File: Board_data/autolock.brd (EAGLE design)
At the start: 65 x 56 mm, 10 parts, among them CN1 RASPBERRYPI-GPIO

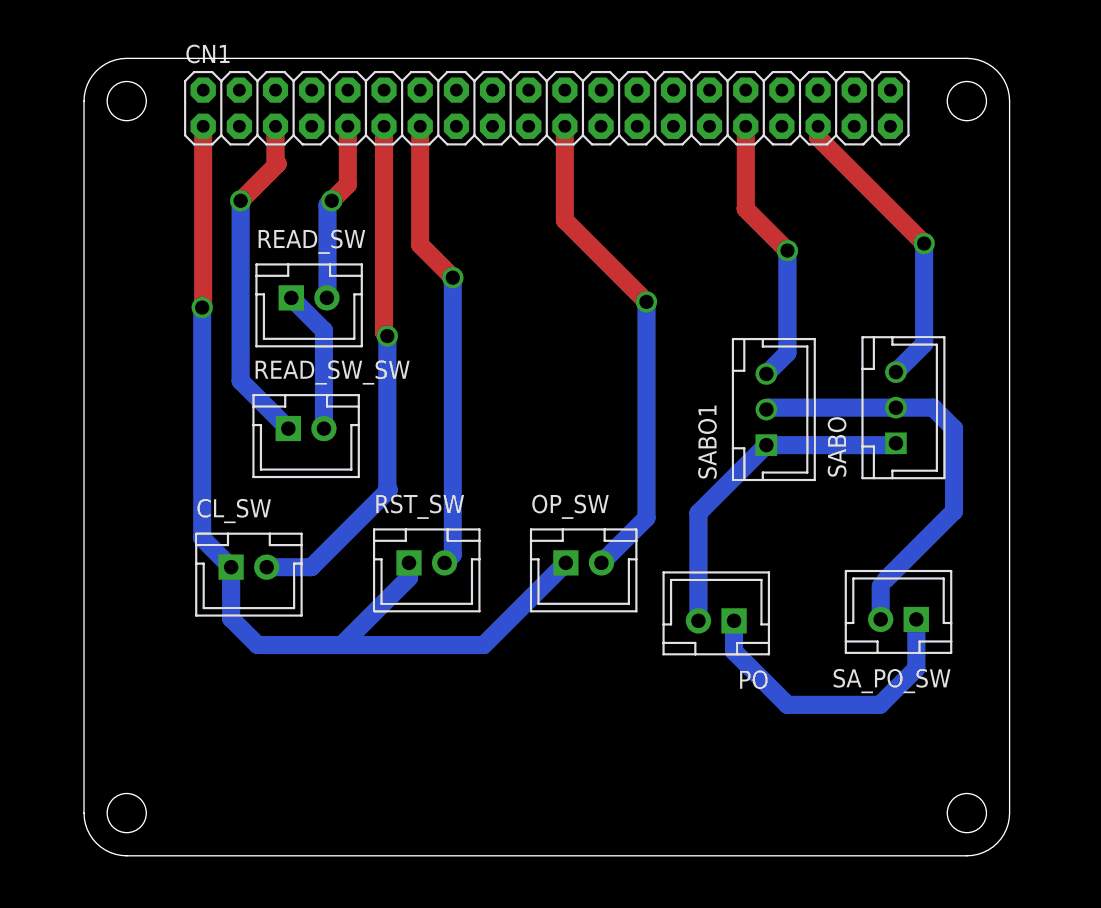
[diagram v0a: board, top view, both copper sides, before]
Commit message: 基板修正・リードスイッチ調整
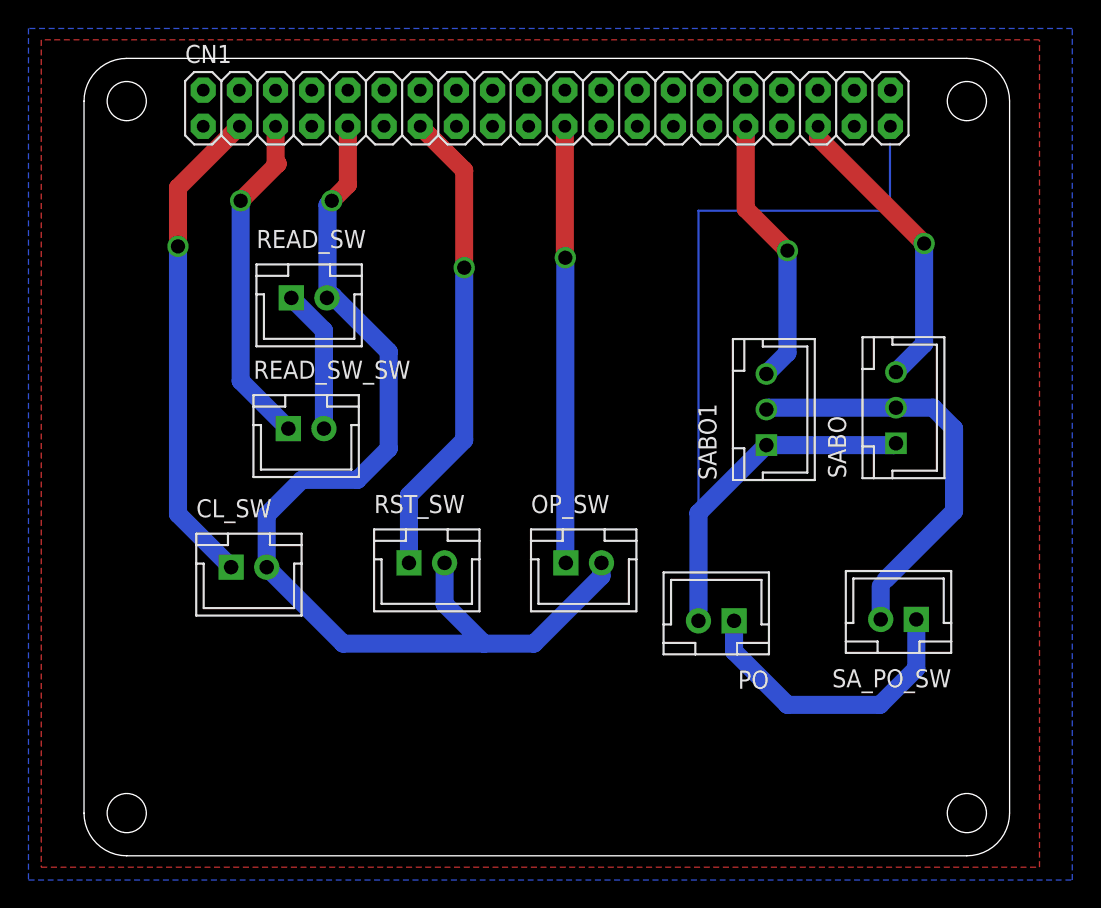
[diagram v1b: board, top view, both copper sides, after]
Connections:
- removed net N$12: PO.2, SABO.1, SABO1.1
- removed net N$4: CN1.9, READ_SW.2
- removed net N$8: CL_SW.2, CN1.11
- removed net N$9: CN1.13, RST_SW.2
- new net GND: CL_SW.2, CN1.39, CN1.9, OP_SW.2, PO.2, READ_SW.2, RST_SW.2, SABO.1, SABO1.1
- new net N$14: CN1.13, RST_SW.1
- net N$1: now also CN1.21; no longer CL_SW.1, CN1.1, RST_SW.1
- net N$2: now also CL_SW.1, CN1.3; no longer CN1.21, OP_SW.2
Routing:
- net GND: track 0.00 -> 145.3 mm, vias 0 -> 1
- net N$1: track 69.8 -> 30.7 mm
- net N$8: track 36.5 -> 0.00 mm, vias 1 -> 0
- net N$14: track 0.00 -> 33.5 mm, vias 0 -> 1
- net N$9: track 31.8 -> 0.00 mm, vias 1 -> 0
- net N$12: track 23.5 -> 0.00 mm
- net N$4: track 12.5 -> 0.00 mm, vias 1 -> 0
- added copper zone on layer 1, net GND
- added copper zone on layer 16, net GND
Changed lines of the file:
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@@
 <signal name="N$1">
 <contactref element="OP_SW" pad="1"/>
-<contactref element="CN1" pad="1"/>
-<contactref element="RST_SW" pad="1"/>
-<contactref element="CL_SW" pad="1"/>
-<wire x1="8.37" y1="51.23" x2="8.37" y2="38.57" width="1.27" layer="1"/>
-<wire x1="8.37" y1="38.57" x2="8.3" y2="38.5" width="1.27" layer="1"/>
-<via x="8.3" y="38.5" extent="1-16" drill="1" diameter="0.3"/>
-<wire x1="8.3" y1="38.5" x2="8.3" y2="22.3" width="1.27" layer="16"/>
-<wire x1="8.3" y1="22.3" x2="10.33" y2="20.27" width="1.27" layer="16"/>
-<wire x1="10.33" y1="20.27" x2="10.33" y2="16.67" width="1.27" layer="16"/>
-<wire x1="10.33" y1="16.67" x2="12.2" y2="14.8" width="1.27" layer="16"/>
-<wire x1="12.2" y1="14.8" x2="18.1" y2="14.8" width="1.27" layer="16"/>
-<wire x1="18.1" y1="14.8" x2="22.82" y2="19.52" width="1.27" layer="16"/>
-<wire x1="22.82" y1="19.52" x2="22.82" y2="20.57" width="1.27" layer="16"/>
-<wire x1="18.1" y1="14.8" x2="28.07" y2="14.8" width="1.27" layer="16"/>
-<wire x1="28.07" y1="14.8" x2="33.84" y2="20.57" width="1.27" layer="16"/>
-</signal>
-<signal name="N$2">
-<contactref element="OP_SW" pad="2"/>
 <contactref element="CN1" pad="21"/>
-<wire x1="33.77" y1="51.23" x2="33.77" y2="44.63" width="1.27" layer="1"/>
-<wire x1="33.77" y1="44.63" x2="39.5" y2="38.9" width="1.27" layer="1"/>
-<via x="39.5" y="38.9" extent="1-16" drill="1" diameter="0.3"/>
-<wire x1="39.5" y1="38.9" x2="39.5" y2="23.73" width="1.27" layer="16"/>
-<wire x1="39.5" y1="23.73" x2="36.34" y2="20.57" width="1.27" layer="16"/>
+<wire x1="33.77" y1="51.23" x2="33.77" y2="42.03" width="1.27" layer="1"/>
+<wire x1="33.77" y1="42.03" x2="33.8" y2="42" width="1.27" layer="1"/>
+<via x="33.8" y="42" extent="1-16" drill="1" diameter="0.3"/>
+<wire x1="33.8" y1="42" x2="33.8" y2="20.61" width="1.27" layer="16"/>
+<wire x1="33.8" y1="20.61" x2="33.84" y2="20.57" width="1.27" layer="16"/>
 </signal>
 <signal name="N$3">
@@
 <wire x1="11" y1="33.35" x2="14.35" y2="30" width="1.27" layer="16"/>
 </signal>
-<signal name="N$4">
-<contactref element="CN1" pad="9"/>
-<wire x1="18.53" y1="51.23" x2="18.53" y2="47.13" width="1.27" layer="1"/>
-<wire x1="18.53" y1="47.13" x2="17.4" y2="46" width="1.27" layer="1"/>
-<via x="17.4" y="46" extent="1-16" drill="1" diameter="0.3"/>
-<wire x1="17.4" y1="46" x2="17.1" y2="45.7" width="1.27" layer="16"/>
-<wire x1="17.1" y1="45.7" x2="17.1" y2="39.32" width="1.27" layer="16"/>
-<contactref element="READ_SW" pad="2"/>
-<wire x1="17.06" y1="39.18" x2="17.1" y2="39.32" width="0" layer="19" extent="16-16"/>
-</signal>
 <signal name="N$7">
 <contactref element="CN1" pad="35"/>
@@
 <wire x1="59" y1="43" x2="59" y2="35.95" width="1.27" layer="16"/>
 <wire x1="59" y1="35.95" x2="57.02" y2="33.97" width="1.27" layer="16"/>
-</signal>
-<signal name="N$9">
-<contactref element="RST_SW" pad="2"/>
-<contactref element="CN1" pad="13"/>
-<wire x1="23.61" y1="51.23" x2="23.61" y2="42.89" width="1.27" layer="1"/>
-<wire x1="23.61" y1="42.89" x2="25.9" y2="40.6" width="1.27" layer="1"/>
-<via x="25.9" y="40.6" extent="1-16" drill="1" diameter="0.3"/>
-<wire x1="25.9" y1="40.6" x2="25.9" y2="21.15" width="1.27" layer="16"/>
-<wire x1="25.9" y1="21.15" x2="25.32" y2="20.57" width="1.27" layer="16"/>
 </signal>
 <signal name="N$6">
@@
 <wire x1="55.95" y1="18.95" x2="56.3" y2="19.4" width="0" layer="19" extent="16-16"/>
 </signal>
-<signal name="N$8">
-<contactref element="CL_SW" pad="2"/>
-<contactref element="CN1" pad="11"/>
-<via x="21.3" y="36.5" extent="1-16" drill="1" diameter="0.3"/>
-<wire x1="12.83" y1="20.27" x2="15.97" y2="20.27" width="1.27" layer="16"/>
-<wire x1="21.4" y1="25.7" x2="15.97" y2="20.27" width="1.27" layer="16"/>
-<wire x1="21.07" y1="51.23" x2="21.07" y2="36.73" width="1.27" layer="1"/>
-<wire x1="21.07" y1="36.73" x2="21.3" y2="36.5" width="1.27" layer="1"/>
-<wire x1="21.3" y1="36.5" x2="21.3" y2="25.8" width="1.27" layer="16"/>
-<wire x1="21.3" y1="25.8" x2="21.4" y2="25.7" width="1.27" layer="16"/>
-</signal>
 <signal name="N$10">
 <contactref element="SABO1" pad="3"/>
@@
 <wire x1="49.4" y1="42.5" x2="49.4" y2="35.3195375" width="1.27" layer="16"/>
 <wire x1="49.4" y1="35.3195375" x2="47.92" y2="33.84" width="1.27" layer="16"/>
-</signal>
-<signal name="N$12">
-<contactref element="SABO" pad="1"/>
-<contactref element="SABO1" pad="1"/>
-<wire x1="57.02" y1="28.97" x2="56.89" y2="28.84" width="1.27" layer="16"/>
-<wire x1="56.89" y1="28.84" x2="47.92" y2="28.84" width="1.27" layer="16"/>
-<contactref element="PO" pad="2"/>
-<wire x1="47.92" y1="28.84" x2="43.15" y2="24.07" width="1.27" layer="16"/>
-<wire x1="43.15" y1="24.07" x2="43.15" y2="16.5" width="1.27" layer="16"/>
 </signal>
 <signal name="N$5">
@@
 <wire x1="16.85" y1="36.89" x2="16.85" y2="30" width="1.27" layer="16"/>
 </signal>
+<signal name="N$14">
+<contactref element="RST_SW" pad="1"/>
+<contactref element="CN1" pad="13"/>
+<wire x1="23.61" y1="51.23" x2="26.7" y2="48.14" width="1.27" layer="1"/>
+<wire x1="26.7" y1="48.14" x2="26.7" y2="41.3" width="1.27" layer="1"/>
+<via x="26.7" y="41.3" extent="1-16" drill="1" diameter="0.3"/>
+<wire x1="26.7" y1="41.3" x2="26.7" y2="29.2" width="1.27" layer="16"/>
+<wire x1="22.82" y1="25.32" x2="22.82" y2="20.57" width="1.27" layer="16"/>
+<wire x1="26.7" y1="29.2" x2="22.82" y2="25.32" width="1.27" layer="16"/>
+</signal>
+<signal name="N$2">
+<contactref element="CL_SW" pad="1"/>
+<contactref element="CN1" pad="3"/>
+<wire x1="10.91" y1="51.23" x2="6.6" y2="46.92" width="1.27" layer="1"/>
+<wire x1="6.6" y1="46.92" x2="6.6" y2="42.8" width="1.27" layer="1"/>
+<via x="6.6" y="42.8" extent="1-16" drill="1" diameter="0.3"/>
+<wire x1="6.6" y1="42.8" x2="6.6" y2="24" width="1.27" layer="16"/>
+<wire x1="6.6" y1="24" x2="10.33" y2="20.27" width="1.27" layer="16"/>
+</signal>
+<signal name="GND">
+<polygon width="0.1524" layer="1" isolate="0.4">
+<vertex x="-3" y="57.3"/>
+<vertex x="-3" y="-0.8"/>
+<vertex x="67.1" y="-0.8"/>
+<vertex x="67.1" y="57.3"/>
+</polygon>
+<polygon width="0.1524" layer="16" isolate="0.4">
+<vertex x="-3.9" y="58.1"/>
+<vertex x="-3.9" y="-1.7"/>
+<vertex x="69.4" y="-1.7"/>
+<vertex x="69.4" y="58.1"/>
+</polygon>
+<contactref element="CN1" pad="9"/>
+<wire x1="18.53" y1="51.23" x2="18.53" y2="47.13" width="1.27" layer="1"/>
+<wire x1="18.53" y1="47.13" x2="17.4" y2="46" width="1.27" layer="1"/>
+<via x="17.4" y="46" extent="1-16" drill="1" diameter="0.3"/>
+<wire x1="17.4" y1="46" x2="17.1" y2="45.7" width="1.27" layer="16"/>
+<wire x1="17.1" y1="39.32" x2="17.1" y2="45.7" width="1.27" layer="16"/>
+<contactref element="READ_SW" pad="2"/>
+<contactref element="CL_SW" pad="2"/>
+<contactref element="OP_SW" pad="2"/>
+<wire x1="12.83" y1="20.27" x2="18.2" y2="14.9" width="1.27" layer="16"/>
+<wire x1="18.2" y1="14.9" x2="28.1" y2="14.9" width="1.27" layer="16"/>
+<wire x1="31.6" y1="14.9" x2="28.1" y2="14.9" width="1.27" layer="16"/>
+<wire x1="31.6" y1="14.9" x2="36.34" y2="19.64" width="1.27" layer="16"/>
+<wire x1="36.34" y1="19.64" x2="36.34" y2="20.57" width="1.27" layer="16"/>
+<wire x1="12.83" y1="20.27" x2="12.83" y2="23.93" width="1.27" layer="16"/>
+<wire x1="15.3" y1="26.4" x2="19.2" y2="26.4" width="1.27" layer="16"/>
+<wire x1="19.2" y1="26.4" x2="21.4" y2="28.6" width="1.27" layer="16"/>
+<wire x1="21.4" y1="28.6" x2="21.4" y2="35.4" width="1.27" layer="16"/>
+<wire x1="21.4" y1="35.4" x2="17.48" y2="39.32" width="1.27" layer="16"/>
+<wire x1="17.48" y1="39.32" x2="17.1" y2="39.32" width="1.27" layer="16"/>
+<wire x1="12.83" y1="23.93" x2="15.3" y2="26.4" width="1.27" layer="16"/>
+<contactref element="RST_SW" pad="2"/>
+<wire x1="25.32" y1="20.57" x2="25.32" y2="17.68" width="1.27" layer="16"/>
+<wire x1="25.32" y1="17.68" x2="28.1" y2="14.9" width="1.27" layer="16"/>
+<contactref element="SABO" pad="1"/>
+<contactref element="SABO1" pad="1"/>
+<wire x1="57.02" y1="28.97" x2="56.89" y2="28.84" width="1.27" layer="16"/>
+<wire x1="56.89" y1="28.84" x2="47.92" y2="28.84" width="1.27" layer="16"/>
+<contactref element="PO" pad="2"/>
+<wire x1="47.92" y1="28.84" x2="43.15" y2="24.07" width="1.27" layer="16"/>
+<wire x1="43.15" y1="24.07" x2="43.15" y2="16.5" width="1.27" layer="16"/>
+<wire x1="56.6" y1="50.0108" x2="56.6" y2="45.3" width="0.1524" layer="16"/>
+<wire x1="43.15" y1="45.3" x2="56.6" y2="45.3" width="0.1524" layer="16"/>
+<contactref element="CN1" pad="39"/>
+<wire x1="43.15" y1="16.5" x2="43.15" y2="45.3" width="0.1524" layer="16"/>
+</signal>
 </signals>
